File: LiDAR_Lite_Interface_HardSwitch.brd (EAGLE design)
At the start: 50.2 x 56.2 mm, 30 parts, among them J1 CONN_6SCREW_2.54, J2 CONN_42.54_SCREW, Q1 2N7002, Q2 2N7002, Q3 DMG3404, Q4 MOSFET_PCH-NX2301P, U1 TLV61220DBV, U2 TS5A23157DGS

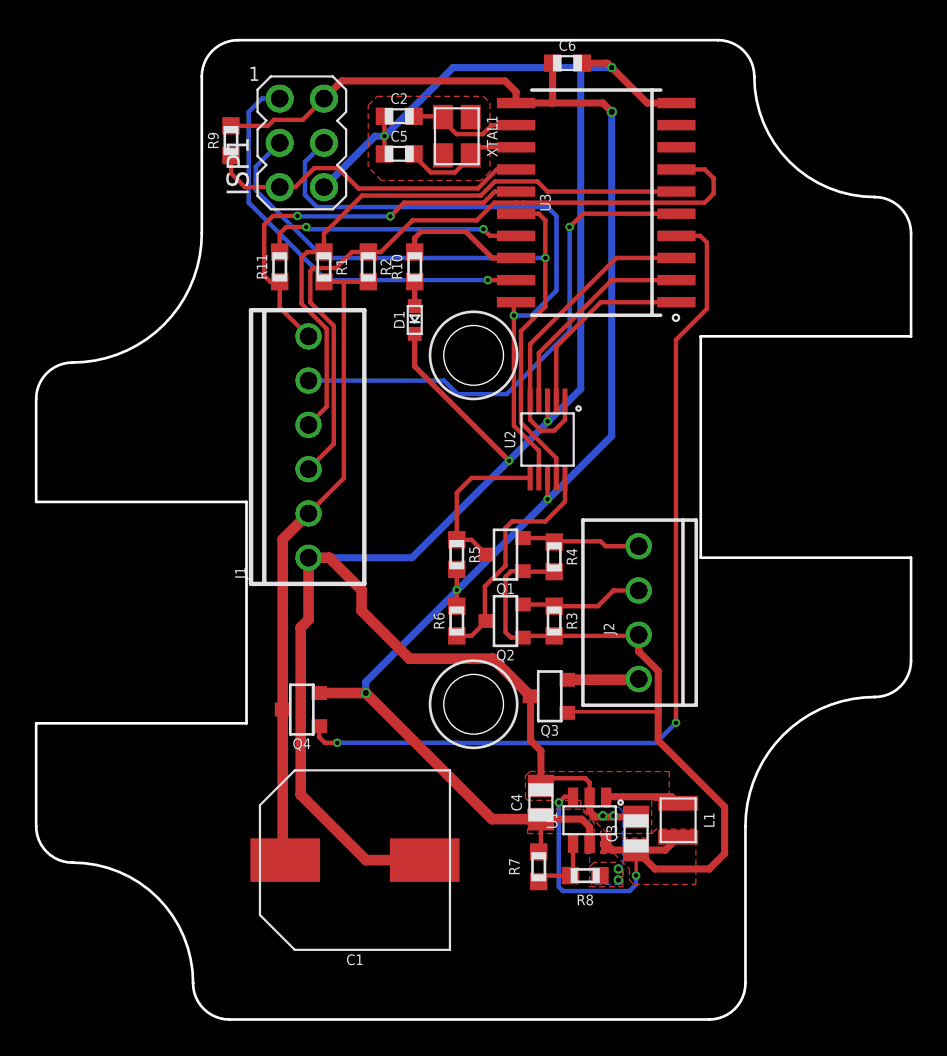
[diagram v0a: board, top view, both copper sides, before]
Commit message: Updated layout, added variants
Improved layout, potentially add button, then ready to send to fab. Added variations of layout for potential future alteration
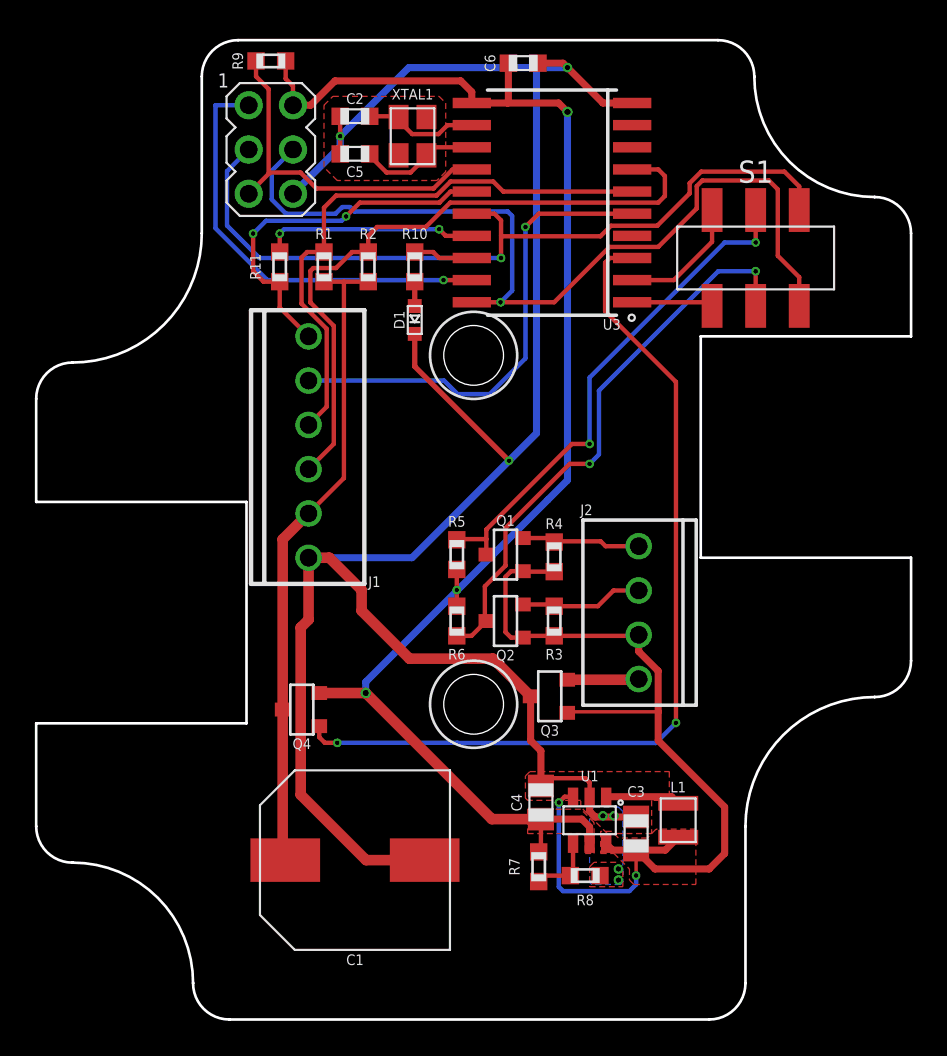
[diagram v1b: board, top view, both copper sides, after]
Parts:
- removed U2: TS5A23157DGS, bschulz:DGS0010A
- added S1: SWITCH_DPDTJS_GULLWING, bschulz:JS202011SCQN
- moved R9 5.11 mm to (13.5, 55.0), turned to 0 degrees
- moved C2 2.54 mm to (18.3, 51.8)
- moved C5 2.54 mm to (18.3, 49.7)
- moved C6 2.54 mm to (27.9, 54.9)
- moved U3 2.54 mm to (29.6, 46.9)
- moved XTAL1 2.54 mm to (21.6, 50.7)
- moved ISP1 1.82 mm to (13.5, 49.9)
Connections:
- removed net OUTPUT_CTRL: U2.1, U2.5, U3.3
- net 5V: no longer U2.8
- net GND: no longer U2.3
- net POWER_SW: now also U3.3; no longer U3.4
- net RX: now also S1.6; no longer U2.4
- net SCL: now also S1.4; no longer U2.9
- net SDA: now also S1.3; no longer U2.7
- net SIG1: now also S1.2; no longer U2.10
- net SIG2: now also S1.5; no longer U2.6
- net TX: now also S1.1; no longer U2.2
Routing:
- net SIG2: track 9.31 -> 29.5 mm, vias 0 -> 2
- net SIG1: track 13.4 -> 32.5 mm, vias 0 -> 2
- net OUTPUT_CTRL: track 18.4 -> 0.00 mm
- net SDA: track 36.4 -> 51.7 mm
- net SCL: track 39.5 -> 46.1 mm
- net TX: track 11.1 -> 4.67 mm
- net 5V: track 90.5 -> 84.4 mm, vias 4 -> 3
- net RX: track 12.4 -> 7.32 mm
- net STAT_LED: track 7.40 -> 3.42 mm
- net MODE_TRIGGER: track 15.0 -> 12.3 mm
- net GND: track 128.8 -> 126.2 mm, vias 8 -> 7
- net SDA_OB: track 40.7 -> 38.4 mm
- net !RESET: track 19.1 -> 20.9 mm
- net MODE: track 23.0 -> 21.3 mm
- net SCL_OB: track 34.8 -> 33.1 mm
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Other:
- board text added: "5V_SW"
- board text added: "EN"
- board text added: "From Logger"
- board text added: "GND"
- board text added: "I2C"
- board text added: "LiDAR Lite Interface"
- board text added: "MODE"
- board text added: "Project-Symbiont-LiDAR v0.0.0 07-12-2019 Bobby Schulz Northern Widget LLC and University of Minnesota"
- board text added: "RX/SCL TX/SDA Vin GND"
- board text added: "SCL"
- board text added: "SDA"
- board text added: "To LiDAR"
- board text added: "UART"

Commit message: Added accel and hall effect, sent to fab
Updated layout, added accelerometer, hall effect switch, generated gerbers and sent to fab
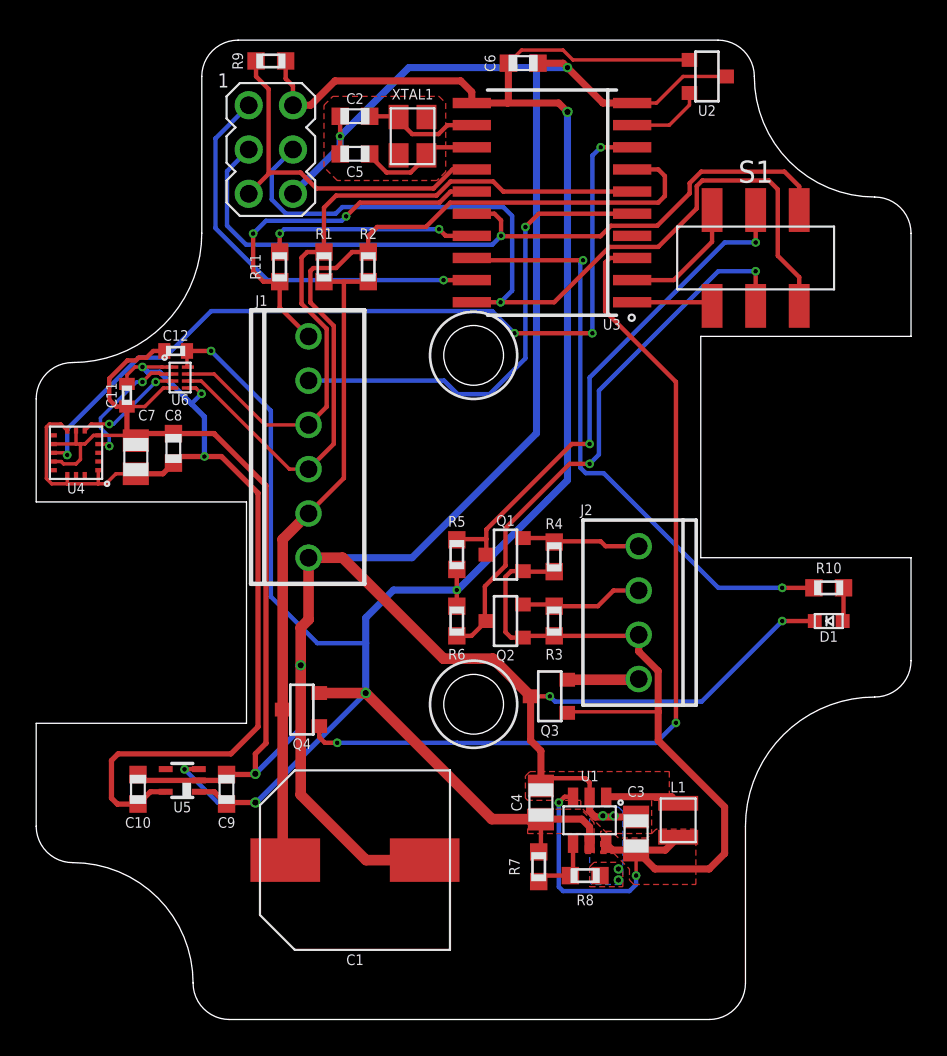
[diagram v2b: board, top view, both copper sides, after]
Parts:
- added C10, C9: 1uF, bschulz_passives:C0603
- added C11, C12: 0.1uF, bschulz_passives:C0402
- added C7: 0.1uF, bschulz_passives:C0805
- added C8: 10uF, bschulz_passives:C0603
- added U2: TCS40DPRSOT23, bschulz:SOT23-3
- added U4: LIS3DHLGA, bschulz:LGA-16
- added U5: MIC53653.3SC70, bschulz:DCK_R-PDSO-G5
- added U6: TXS0102DQM, bschulz:DQM_R-PX2SON-N8
- moved R10 30.1 mm to (45.5, 24.8), turned to 180 degrees
- moved D1 29.4 mm to (45.5, 22.9), turned to 0 degrees
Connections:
- new net 3V3: C10.1, C11.1, C7.1, C8.1, U4.1, U4.14, U4.8, U5.5, U6.1, U6.5
- new net ACCEL_INT: U3.8, U4.11
- new net SCL_OB_LV: U4.4, U6.2
- new net SDA_OB_LV: U4.6, U6.3
- new net SWITCH_OUT: U2.2, U3.9
- net 5V: now also C12.1, C9.1, U2.1, U5.1, U5.3, U6.8
- net GND: now also C10.2, C11.2, C12.2, C7.2, C8.2, C9.2, U2.3, U4.10, U4.12, U4.5, U4.7, U5.2, U6.4
- net SCL_OB: now also U6.7
- net SDA_OB: now also U6.6
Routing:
- net GND: track 126.2 -> 200.2 mm, vias 7 -> 10
- net 3V3: track 0.00 -> 60.1 mm, vias 0 -> 3
- net 5V: track 84.4 -> 140.0 mm, vias 3 -> 6
- net ACCEL_INT: track 0.00 -> 48.4 mm, vias 0 -> 4
- net STAT_LED: track 3.42 -> 34.7 mm, vias 0 -> 2
- net SDA_OB: track 38.4 -> 47.4 mm
- net SCL_OB: track 33.1 -> 41.3 mm
- net SCL_OB_LV: track 0.00 -> 7.71 mm, vias 0 -> 2
- net SDA_OB_LV: track 0.00 -> 6.20 mm, vias 0 -> 2
- net SWITCH_OUT: track 0.00 -> 4.46 mm
- net SCL: track 46.1 -> 44.7 mm
- net MISO: track 24.9 -> 23.8 mm
- net N$4: track 1.40 -> 1.93 mm
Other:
- board text added: "Black"
- board text added: "Blue"
- board text added: "Green"
- board text added: "Orange"
- board text added: "Red"
- board text added: "Yellow"

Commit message: Minor value updates, generated BoM
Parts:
- C1: value (none) -> 680uF
- C2, C5: value (none) -> 10pF
- C7: value 0.1uF -> 10uF
- C8: value 10uF -> 0.1uF
- R10: value (none) -> 330
- R3, R4, R5, R6: value (none) -> 10k
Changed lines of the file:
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@@
 <grid distance="50" unitdist="mil" unit="mm" style="lines" multiple="1" display="no" altdistance="5" altunitdist="mil" altunit="mm"/>
 <layers>
-<layer number="1" name="Top" color="4" fill="1" visible="yes" active="yes"/>
+<layer number="1" name="Top" color="4" fill="1" visible="no" active="yes"/>
 <layer number="2" name="Route2" color="16" fill="1" visible="no" active="no"/>
 <layer number="3" name="Route3" color="17" fill="1" visible="no" active="no"/>
@@
 <layer number="14" name="Route14" color="22" fill="1" visible="no" active="no"/>
 <layer number="15" name="Route15" color="23" fill="1" visible="no" active="no"/>
-<layer number="16" name="Bottom" color="1" fill="1" visible="yes" active="yes"/>
+<layer number="16" name="Bottom" color="1" fill="1" visible="no" active="yes"/>
 <layer number="17" name="Pads" color="2" fill="1" visible="yes" active="yes"/>
 <layer number="18" name="Vias" color="2" fill="1" visible="yes" active="yes"/>
@@
 <layer number="21" name="tPlace" color="7" fill="1" visible="yes" active="yes"/>
 <layer number="22" name="bPlace" color="7" fill="1" visible="no" active="yes"/>
-<layer number="23" name="tOrigins" color="15" fill="1" visible="no" active="yes"/>
+<layer number="23" name="tOrigins" color="15" fill="1" visible="yes" active="yes"/>
 <layer number="24" name="bOrigins" color="15" fill="1" visible="no" active="yes"/>
 <layer number="25" name="tNames" color="7" fill="1" visible="yes" active="yes"/>
@@
 <attribute name="VALUE_PART" value="4.7k" x="19.05" y="43.18" size="1.778" layer="27" rot="R270" display="off"/>
 </element>
-<element name="C1" library="bschulz_passives" package="UW-10X10_NICHICON" value="" x="18.288" y="9.144" smashed="yes" rot="R90">
+<element name="C1" library="bschulz_passives" package="UW-10X10_NICHICON" value="680uF" x="18.288" y="9.144" smashed="yes" rot="R90">
 <attribute name="DIGIKEY" value="493-2182-1-ND" x="18.288" y="9.144" size="1.778" layer="27" rot="R90" display="off"/>
 <attribute name="MF" value="Nichicon" x="18.288" y="9.144" size="1.778" layer="27" rot="R90" display="off"/>
@@
 <attribute name="VALUE" x="26.924" y="24.511" size="0.6096" layer="27" font="vector" ratio="20" rot="R180" align="top-center"/>
 </element>
-<element name="R3" library="bschulz_passives" package="R0603" value="" x="29.718" y="22.86" smashed="yes" rot="R270">
+<element name="R3" library="bschulz_passives" package="R0603" value="10k" x="29.718" y="22.86" smashed="yes" rot="R270">
 <attribute name="DIGIKEY" value="311-10.0KHRCT-ND" x="29.718" y="22.86" size="1.778" layer="27" rot="R270" display="off"/>
 <attribute name="MF" value="Yageo" x="29.718" y="22.86" size="1.778" layer="27" rot="R270" display="off"/>
@@
 <attribute name="VALUE_PART" value="10k" x="29.718" y="22.86" size="1.778" layer="27" rot="R270" display="off"/>
 </element>
-<element name="R4" library="bschulz_passives" package="R0603" value="" x="29.718" y="26.543" smashed="yes" rot="R270">
+<element name="R4" library="bschulz_passives" package="R0603" value="10k" x="29.718" y="26.543" smashed="yes" rot="R270">
 <attribute name="DIGIKEY" value="311-10.0KHRCT-ND" x="29.718" y="26.543" size="1.778" layer="27" rot="R270" display="off"/>
 <attribute name="MF" value="Yageo" x="29.718" y="26.543" size="1.778" layer="27" rot="R270" display="off"/>
@@
 <attribute name="VALUE_PART" value="10k" x="29.718" y="26.543" size="1.778" layer="27" rot="R270" display="off"/>
 </element>
-<element name="R5" library="bschulz_passives" package="R0603" value="" x="24.13" y="26.67" smashed="yes" rot="R270">
+<element name="R5" library="bschulz_passives" package="R0603" value="10k" x="24.13" y="26.67" smashed="yes" rot="R270">
 <attribute name="DIGIKEY" value="311-10.0KHRCT-ND" x="24.13" y="26.67" size="1.778" layer="27" rot="R270" display="off"/>
 <attribute name="MF" value="Yageo" x="24.13" y="26.67" size="1.778" layer="27" rot="R270" display="off"/>
@@
 <attribute name="VALUE_PART" value="10k" x="24.13" y="26.67" size="1.778" layer="27" rot="R270" display="off"/>
 </element>
-<element name="R6" library="bschulz_passives" package="R0603" value="" x="24.13" y="22.86" smashed="yes" rot="R90">
+<element name="R6" library="bschulz_passives" package="R0603" value="10k" x="24.13" y="22.86" smashed="yes" rot="R90">
 <attribute name="DIGIKEY" value="311-10.0KHRCT-ND" x="24.13" y="22.86" size="1.778" layer="27" rot="R90" display="off"/>
 <attribute name="MF" value="Yageo" x="24.13" y="22.86" size="1.778" layer="27" rot="R90" display="off"/>
@@
 <attribute name="NAME" x="21.59" y="53.086" size="0.6096" layer="25" font="vector" ratio="15" align="center"/>
 </element>
-<element name="C2" library="bschulz_passives" package="C0603" value="" x="18.288" y="51.816" smashed="yes">
+<element name="C2" library="bschulz_passives" package="C0603" value="10pF" x="18.288" y="51.816" smashed="yes">
 <attribute name="DIGIKEY" value="311-1058-1-ND" x="18.288" y="51.816" size="1.778" layer="27" display="off"/>
 <attribute name="MF" value="Yageo" x="18.288" y="51.816" size="1.778" layer="27" display="off"/>
@@
 <attribute name="VALUE" x="18.288" y="50.8" size="0.6096" layer="27" font="vector" ratio="15" align="center"/>
 </element>
-<element name="C5" library="bschulz_passives" package="C0603" value="" x="18.288" y="49.657" smashed="yes">
+<element name="C5" library="bschulz_passives" package="C0603" value="10pF" x="18.288" y="49.657" smashed="yes">
 <attribute name="DIGIKEY" value="311-1058-1-ND" x="18.288" y="49.657" size="1.778" layer="27" display="off"/>
 <attribute name="MF" value="Yageo" x="18.288" y="49.657" size="1.778" layer="27" display="off"/>
@@
 <attribute name="NAME" x="45.466" y="21.971" size="0.6096" layer="21" font="vector" ratio="15" align="center"/>
 </element>
-<element name="R10" library="bschulz_passives" package="R0603" value="" x="45.466" y="24.765" smashed="yes" rot="R180">
+<element name="R10" library="bschulz_passives" package="R0603" value="330" x="45.466" y="24.765" smashed="yes" rot="R180">
 <attribute name="DIGIKEY" value="311-330HRCT-ND" x="45.466" y="28.575" size="1.778" layer="27" rot="R180" display="off"/>
 <attribute name="MF" value="Yageo" x="45.466" y="28.575" size="1.778" layer="27" rot="R180" display="off"/>
@@
 <attribute name="NAME" x="2.286" y="30.48" size="0.6096" layer="25" font="vector" ratio="15" rot="R180" align="center"/>
 </element>
-<element name="C7" library="bschulz_passives" package="C0805" value="0.1uF" x="5.715" y="32.258" smashed="yes" rot="R90">
+<element name="C7" library="bschulz_passives" package="C0805" value="10uF" x="5.715" y="32.258" smashed="yes" rot="R90">
 <attribute name="DIGIKEY" value="490-6473-6-ND" x="5.715" y="32.258" size="1.778" layer="27" rot="R90" display="off"/>
 <attribute name="MF" value="Murata" x="5.715" y="32.258" size="1.778" layer="27" rot="R90" display="off"/>
@@
 <attribute name="VALUE" x="7.112" y="32.258" size="0.6096" layer="27" font="vector" ratio="15" rot="R90" align="center"/>
 </element>
-<element name="C8" library="bschulz_passives" package="C0603" value="10uF" x="7.874" y="32.766" smashed="yes" rot="R90">
+<element name="C8" library="bschulz_passives" package="C0603" value="0.1uF" x="7.874" y="32.766" smashed="yes" rot="R90">
 <attribute name="DIGIKEY" value="490-6051-1-ND" x="7.874" y="32.766" size="1.778" layer="27" rot="R90" display="off"/>
 <attribute name="MF" value="Murata" x="7.874" y="32.766" size="1.778" layer="27" rot="R90" display="off"/>
